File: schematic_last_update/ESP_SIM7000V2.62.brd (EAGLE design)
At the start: 89.7 x 57.9 mm, 72 parts, among them J1 U.FL-R-SMT(01), J2 U.FL-R-SMT(01), J3 78646-3001, Q1 SI2305CDS, Q2 BSS138, Q3 SI2305CDS, Q4 BSS138, Q5 SI2305CDS, Q6 BSS138, Q7 BSS138, Q8 BSS138, Q9 BSS138, U1 ESP-WROOM-03, U3 TXB0104D, U4 MIC5239S, X1 S2B-PH-K-S, X2 B2B-PH-K-S

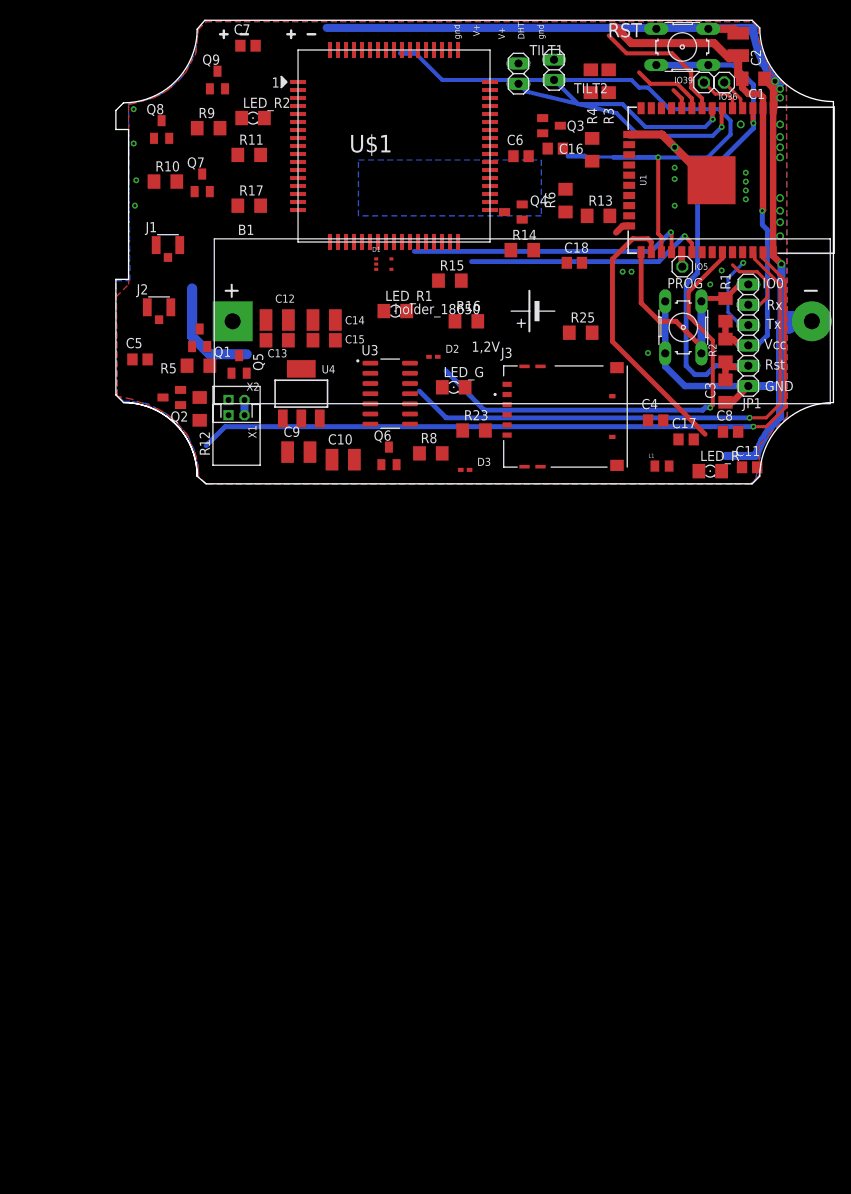
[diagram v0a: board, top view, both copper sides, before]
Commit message: Correction schematic et ajout de TXB0108PWR
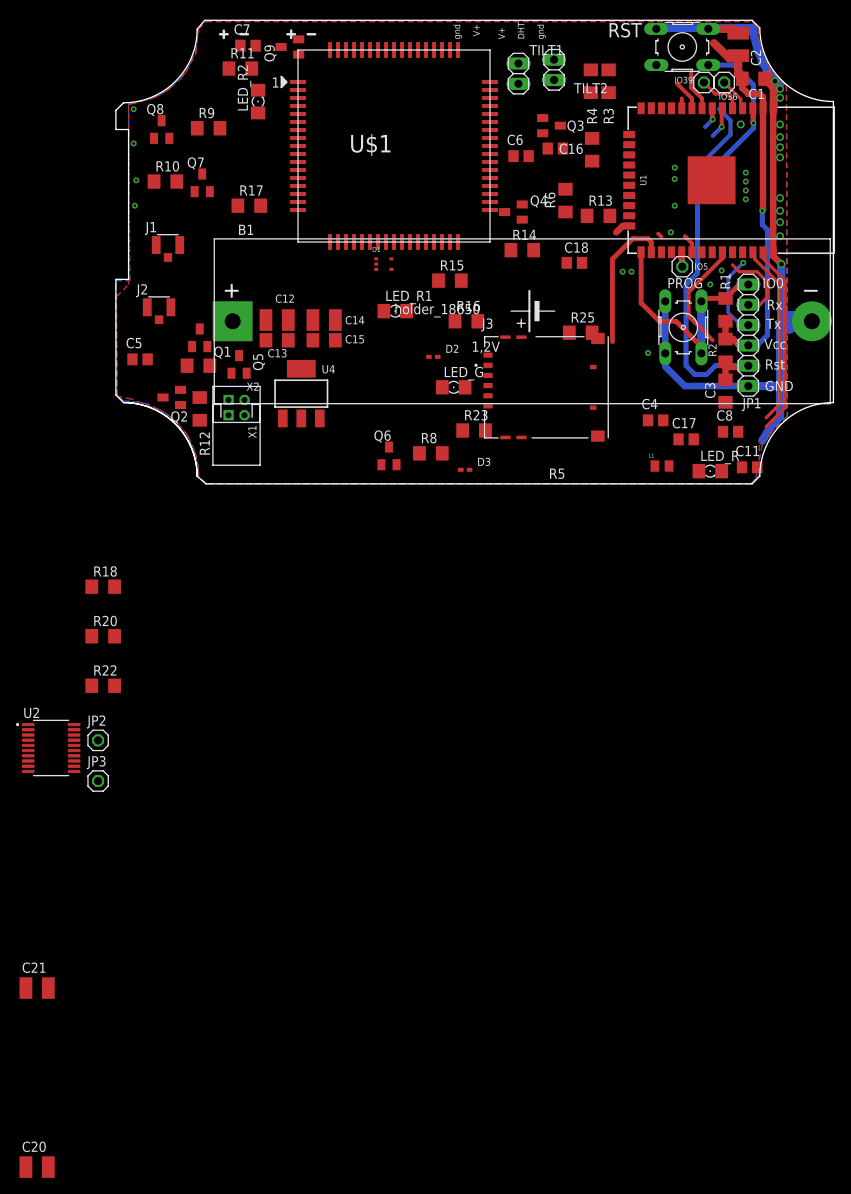
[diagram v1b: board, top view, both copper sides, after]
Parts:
- removed C10, C9: 0.1uF, eagle-ltspice:C1210
- removed U3: TXB0104D, TXB0104D:SOIC127P600X175-14N
- added C20, C21: 0.1uF, eagle-ltspice:C1210
- added JP2, JP3: (no value), pinhead:1X01
- added R18, R20: NC, eagle-ltspice:R1206
- added R22: 10k, eagle-ltspice:R1206
- added U2: TXB0108PWR, TXB0108PWR:SOP65P640X120-20N
- moved R11 10.9 mm to (17.6, 53.5)
- moved Q9 9.95 mm to (23.8, 56.2), turned to 90 degrees
- moved J3 4.36 mm to (55.9, 13.7)
- moved LED_R2 2.16 mm to (19.8, 49.4), turned to 90 degrees
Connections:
- removed net LTE_DRT: U3.5
- removed net SCL: R16.1, R17.2, U1.36
- removed net SDA: R14.1, R15.2, U1.33
- new net LTE_SCL: R16.1, R17.2, U2.7
- new net LTE_SDA: R14.1, R15.2, U2.6
- new net N$42: R18.2, U$1.P$25
- new net N$43: R22.2
- new net N$44: U$1.P$34
- new net N$45: JP3.1, U$1.P$23
- new net UC_SCL: U1.36, U2.14
- new net UC_SDA: U1.33, U2.15
- new net VDD: Q3.3
- net +1V8: now also C21.2, R15.1, R17.1, U2.10, U2.2; no longer C9.2, U$1.P$23, U3.1, U3.8
- net +3V3: no longer R15.1
- net +5V: now also C20.2, U2.19; no longer C10.2, U3.14
- net GND: now also C20.1, C21.1, LED_R2.A, R18.1, R22.1, U2.11; no longer C10.1, C9.1, U3.7
- net LTE_RI: no longer U3.4
- net LTE_RXD: no longer U3.2
- net LTE_TXD: no longer U3.3
- net N$34: now also R20.1; no longer LED_R2.A
- net UC_DRT: now also U2.16; no longer U3.10
- net UC_RI: now also U2.17; no longer U3.11
- net UC_RX: now also U2.20; no longer U3.13
- net UC_TX: now also U2.18; no longer U3.12
- net V+: no longer Q3.3, R17.1
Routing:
- net MEASURE: track 80.1 -> 8.38 mm, vias 1 -> 0
- net POWER: track 94.9 -> 23.9 mm, vias 1 -> 0
- net SCL: track 67.5 -> 0.00 mm, vias 1 -> 0
- net GND: track 162.5 -> 99.9 mm, vias 30 -> 29
- net SDA: track 58.2 -> 0.00 mm, vias 1 -> 0
- net UC_RX: track 35.6 -> 0.09 mm
- net UC_TX: track 30.4 -> 2.37 mm, vias 1 -> 0
- net TILT1: track 30.1 -> 3.95 mm
- net UC_SCL: track 0.00 -> 22.8 mm
- net TILT2: track 24.1 -> 2.76 mm
- net NEXT: track 34.1 -> 17.7 mm
- net UC_SDA: track 0.00 -> 14.5 mm
- net V+: track 13.7 -> 0.00 mm
- net +3V3: track 62.9 -> 49.7 mm
- net DHT: track 17.3 -> 5.05 mm
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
